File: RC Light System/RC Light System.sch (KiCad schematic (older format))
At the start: 13 parts, among them J1 OUTPUT, J2 OUTPUT, J3 STR_IN, J4 STR_OUT, J5 THR_IN, J6 THR_OUT, J7 AUX_IN, J8 AUX_OUT, J9 VBATT

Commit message: First layout done
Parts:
- added J10: BIND_IN, Connector_PinSocket_2.54mm:PinSocket_1x03_P2.54mm_Vertical, symbol rc_light_system:Conn_Channel_Input
- added JP1: BIND, Connector_PinHeader_2.54mm:PinHeader_1x02_P2.54mm_Vertical, symbol Device:Jumper_NO_Small
- J1: value OUTPUT -> OUTPUT 1
- J2: value OUTPUT -> OUTPUT 2
- R1, R2: footprint resistor:R_Axial_DIN0207_L6.3mm_D2.5mm_P10.16mm_Horizontal -> resistor:R_Axial_DIN0207_L6.3mm_D2.5mm_P7.62mm_Horizontal
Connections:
- net AUX: now also A1.17 (D18); no longer A1.14 (D16)
- net GND: now also J10.1 (GND), JP1.1
- net SER_DATA: now also A1.11 (D8); no longer A1.7 (D4)
- net SER_LATCH: now also A1.7 (D4); no longer A1.11 (D8)
- net SER_CLK_2: now reaches A1.8 (D5)
- net SER_CLK_2: now also J2.5 (CLOCK)
- net BEC: now reaches J3.2 (BEC), J4.2 (BEC)
- net BEC: now also J5.2 (BEC), J6.2 (BEC), J7.2 (BEC), J8.2 (BEC)
- net SER_CLK renamed SER_CLK_1
- net SER_CLK_1: no longer J2.5 (CLOCK)
- new net: J10.3 (VCC), JP1.2
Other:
- moved on the sheet: A1, D1, J1, J2, J3, J4, J5, J6, J7, J8, J9, R1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

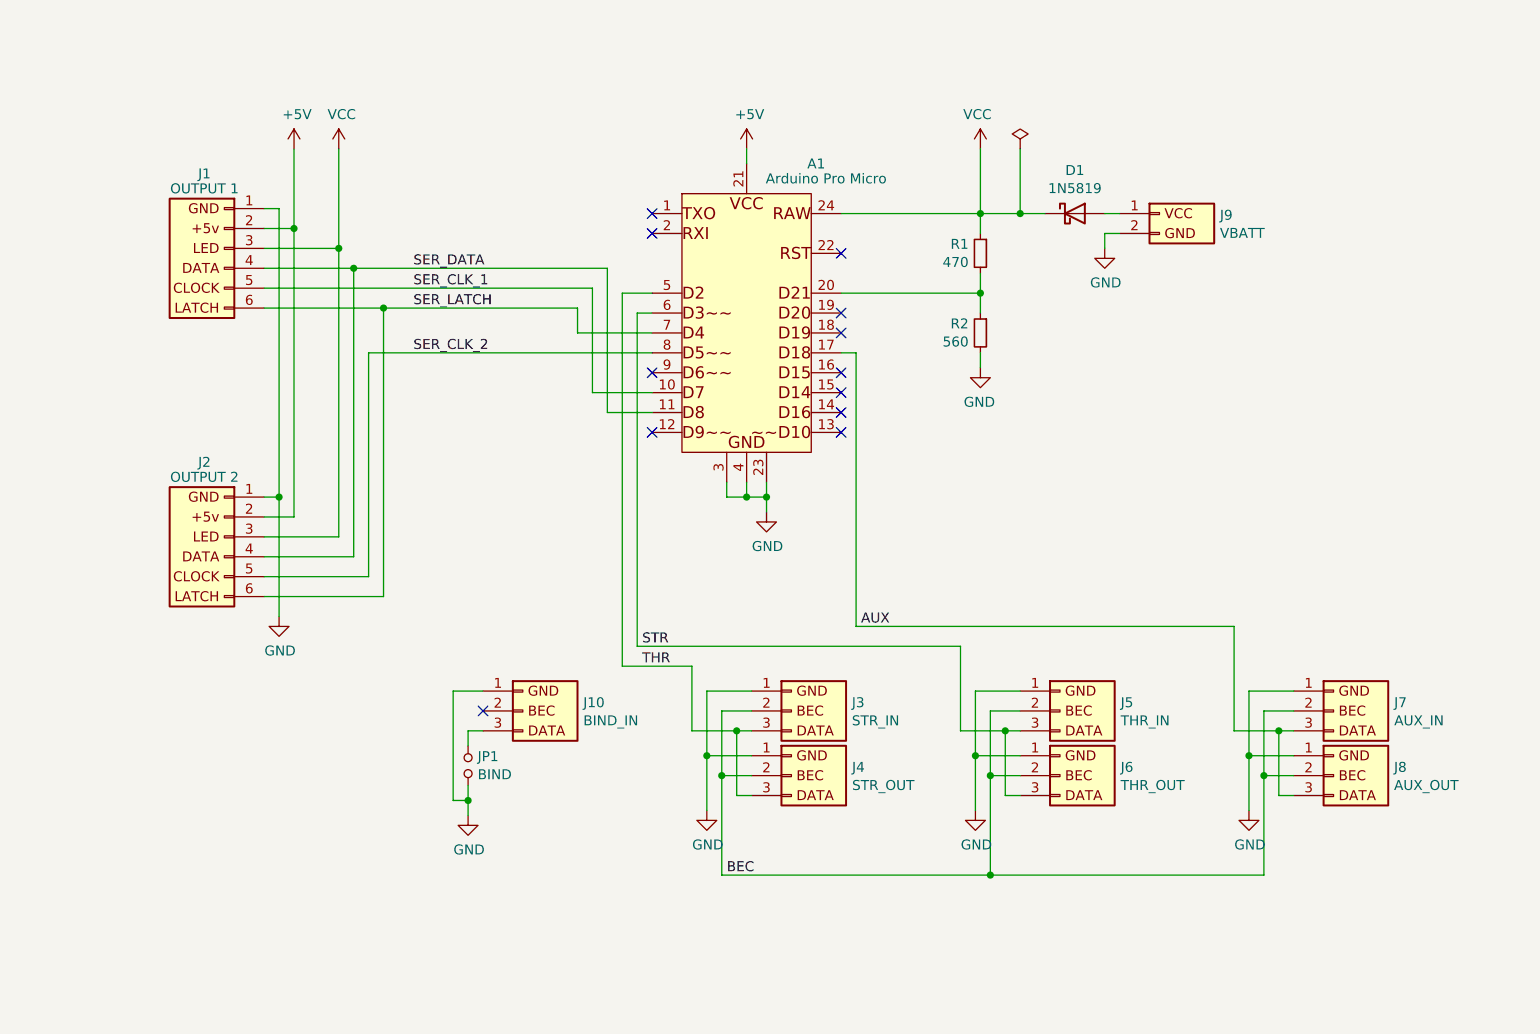
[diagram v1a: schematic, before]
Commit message: Added voltage dividers
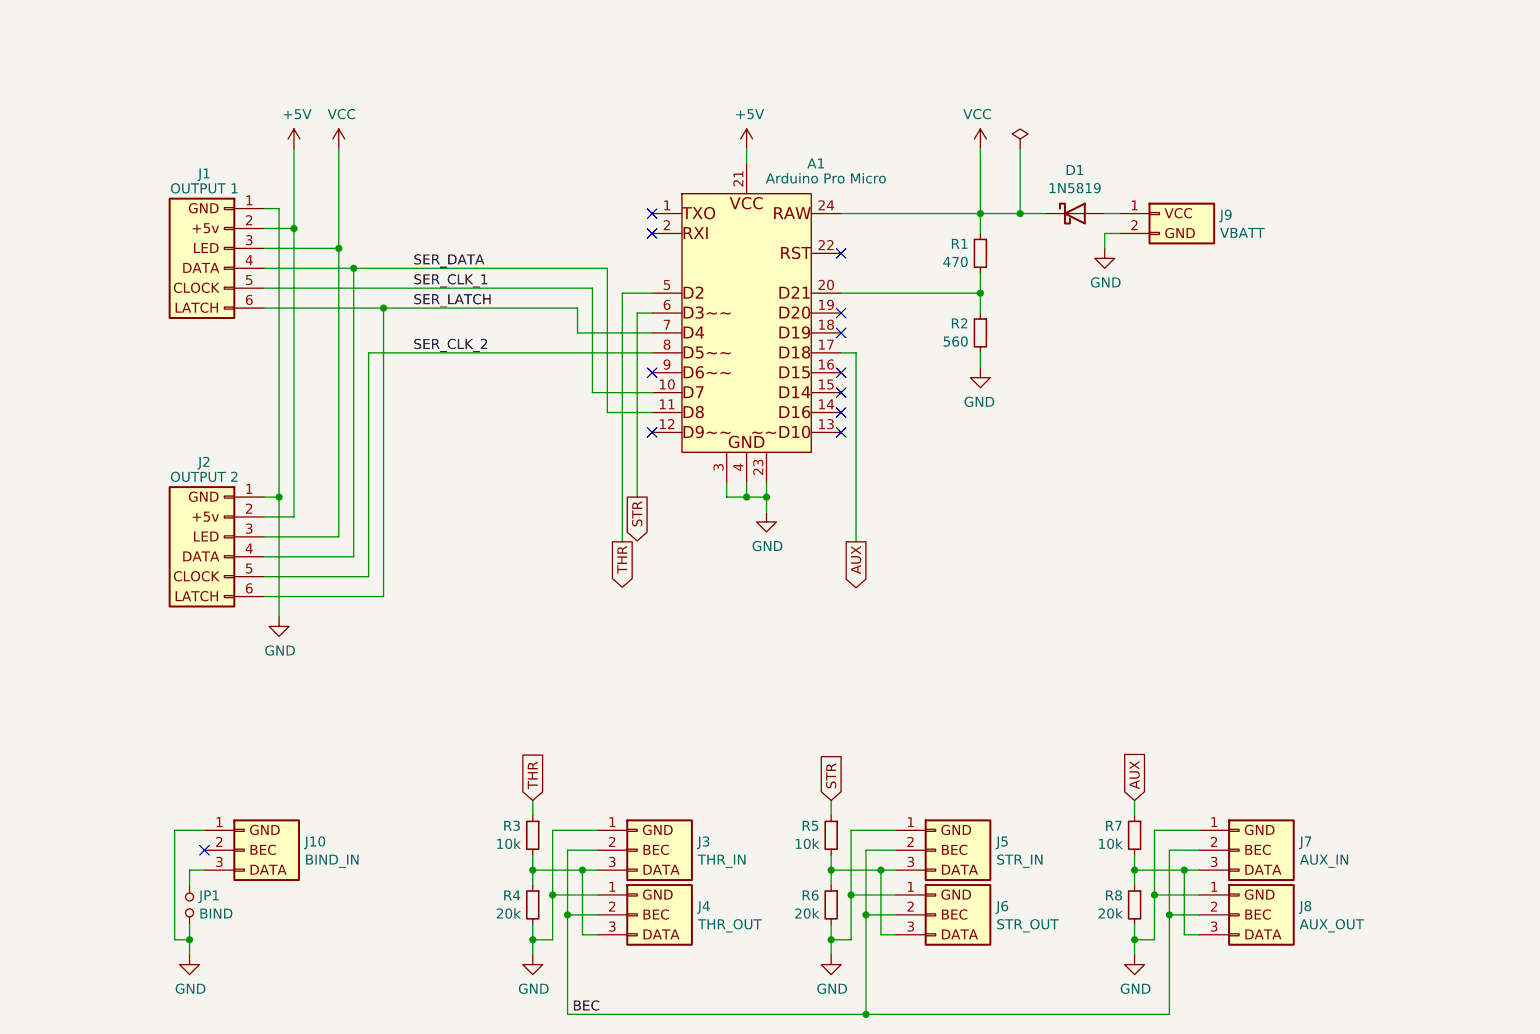
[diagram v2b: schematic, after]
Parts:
- added R3, R5, R7: 10k, resistor:R_Axial_DIN0207_L6.3mm_D2.5mm_P7.62mm_Horizontal, symbol Device:R_Small
- added R4, R6, R8: 20k, resistor:R_Axial_DIN0207_L6.3mm_D2.5mm_P7.62mm_Horizontal, symbol Device:R_Small
- J3: value STR_IN -> THR_IN
- J4: value STR_OUT -> THR_OUT
- J5: value THR_IN -> STR_IN
- J6: value THR_OUT -> STR_OUT
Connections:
- net AUX: now also R7.1; no longer J7.3 (VCC), J8.3 (VCC)
- net GND: now also R4.2, R6.2, R8.2
- net STR: now also R5.1; no longer J5.3 (VCC), J6.3 (VCC)
- net THR: now also R3.1; no longer J3.3 (VCC), J4.3 (VCC)
- new net: J3.3 (VCC), J4.3 (VCC), R3.2, R4.1
- new net: J5.3 (VCC), J6.3 (VCC), R5.2, R6.1
- new net: J7.3 (VCC), J8.3 (VCC), R7.2, R8.1
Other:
- moved on the sheet: J10, J3, J4, J5, J6, J7, J8, JP1

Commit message: Simplified power to use 5/6v
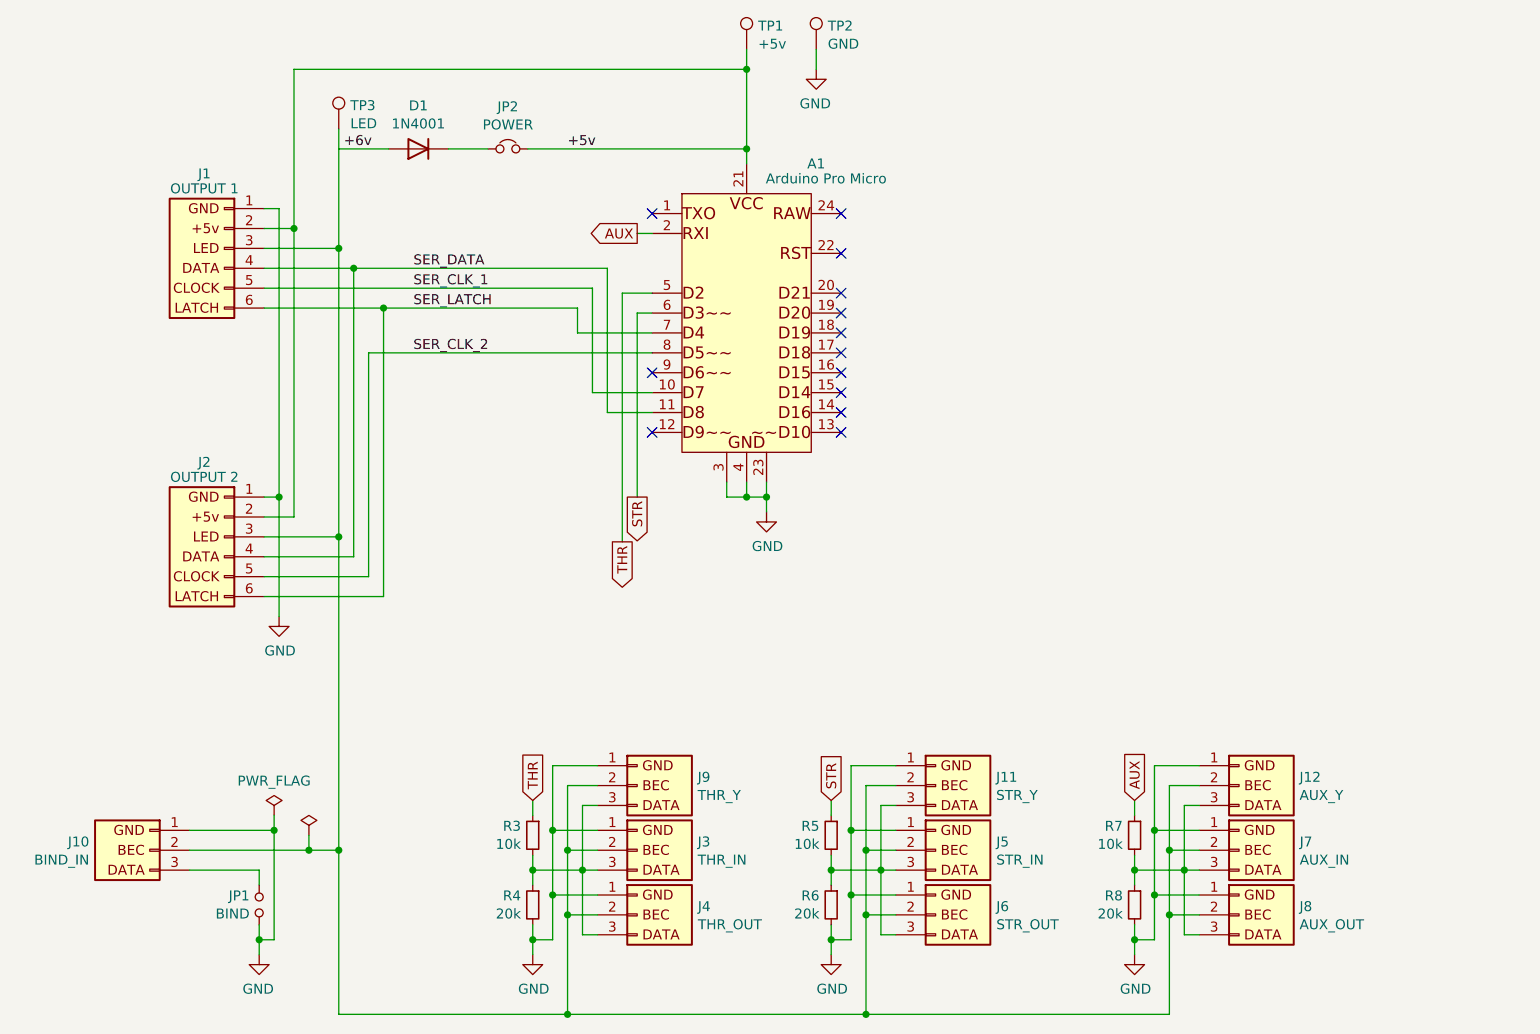
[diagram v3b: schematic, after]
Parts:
- removed D1: 1N5819, Diode_THT:D_DO-41_SOD81_P10.16mm_Horizontal, symbol Diode:1N5819
- removed J9: VBATT, rc_light_system:Conn_Light_Power, symbol rc_light_system:Conn_Light_Power
- removed R1: 470, resistor:R_Axial_DIN0207_L6.3mm_D2.5mm_P7.62mm_Horizontal, symbol Device:R_Small
- removed R2: 560, resistor:R_Axial_DIN0207_L6.3mm_D2.5mm_P7.62mm_Horizontal, symbol Device:R_Small
- added D1: 1N4001, Diode_THT:D_DO-41_SOD81_P10.16mm_Horizontal, symbol Diode:1N4001
- added J11: STR_Y, Connector_PinHeader_2.54mm:PinHeader_1x03_P2.54mm_Vertical, symbol rc_light_system:Conn_Channel_Output
- added J12: AUX_Y, Connector_PinHeader_2.54mm:PinHeader_1x03_P2.54mm_Vertical, symbol rc_light_system:Conn_Channel_Output
- added J9: THR_Y, Connector_PinHeader_2.54mm:PinHeader_1x03_P2.54mm_Vertical, symbol rc_light_system:Conn_Channel_Output
- added JP2: POWER, solder_bridge:bridge, symbol Device:Jumper_NC_Small
- added TP1: +5v, rc_light_system:Testpoint, symbol Connector:TestPoint
- added TP2: GND, rc_light_system:Testpoint, symbol Connector:TestPoint
- added TP3: LED, rc_light_system:Testpoint, symbol Connector:TestPoint
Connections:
- net BEC is gone; now on net +6v: J3.2 (BEC), J4.2 (BEC), J5.2 (BEC), J6.2 (BEC), J7.2 (BEC), J8.2 (BEC)
- net AUX: now also A1.2 (RXI); no longer A1.17 (D18)
- net GND: now also J11.1 (GND), J12.1 (GND), J9.1 (GND), TP2.1
- net +6v: now reaches J10.2 (BEC)
- net +6v: now also J1.3 (LED), J2.3 (LED), D1.2 (A), J11.2 (BEC), J12.2 (BEC), J9.2 (BEC), TP3.1
- net at J3.3 (VCC), J4.3 (VCC), R3.2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: now also J9.3 (VCC)
- net at J5.3 (VCC), J6.3 (VCC), R5.2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: now also J11.3 (VCC)
- net at J7.3 (VCC), J8.3 (VCC), R7.2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: now also J12.3 (VCC)
- net +5V renamed +5v
- net +5v: now also JP2.2, TP1.1
- removed net VCC: A1.24 (RAW), J1.3 (LED), J2.3 (LED)
- new net: D1.1 (K), JP2.1
- no-connect marks 12 -> 13
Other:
- moved on the sheet: J10, JP1
